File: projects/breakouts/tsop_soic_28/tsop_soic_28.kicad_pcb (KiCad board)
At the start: 2 copper layers, 35.6 x 17.8 mm, 6 parts, among them K1 PINS_28, K2 PINS_14, K3 PINS_14, K4 PINS_28

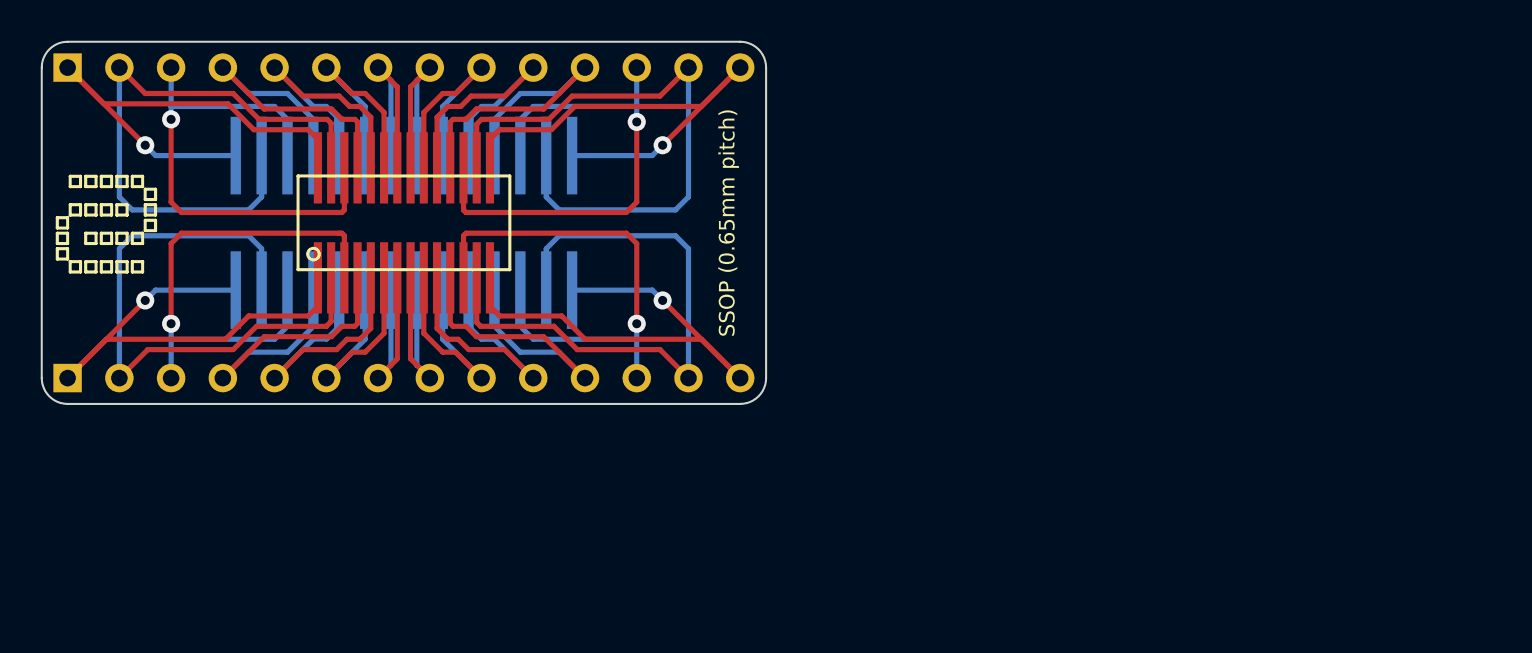
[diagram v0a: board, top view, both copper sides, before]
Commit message: Move breakouts to separate folder; rename tsop to tsop/soic
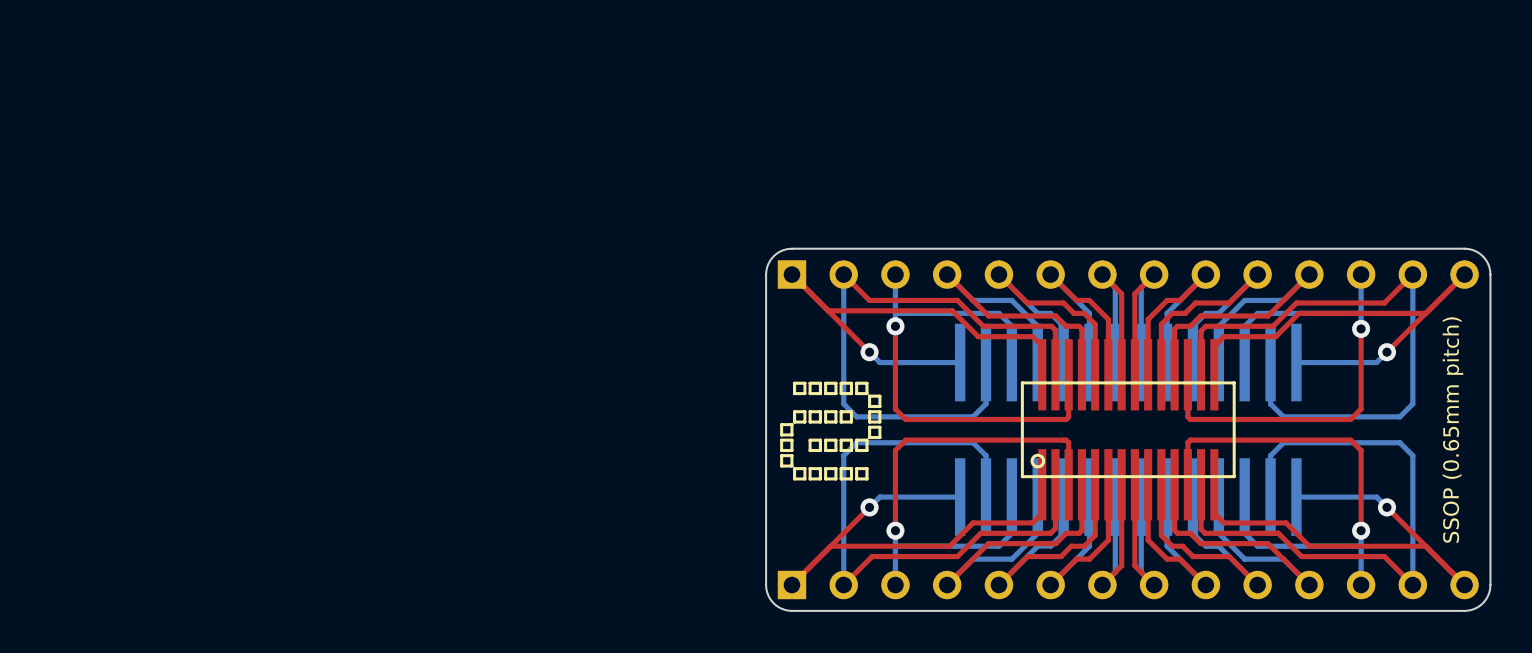
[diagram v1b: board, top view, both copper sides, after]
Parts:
- moved VAL 37.0 mm to (59.1, 45.7) (x2)
- moved K1 37.0 mm to (73.7, 45.7)
- moved K2 37.0 mm to (73.7, 53.3)
- moved K3 37.0 mm to (73.7, 38.1)
- moved K4 37.0 mm to (73.7, 45.7)
